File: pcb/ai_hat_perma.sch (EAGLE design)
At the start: 285 parts, among them J1 1X01-SM, J10 1X01-SM, J100 1X01-SM, J101 1X01-SM, J102 1X01-SM, J103 1X01-SM, J104 1X01-SM, J105 1X01-SM, J106 1X01-SM, J107 1X01-SM, J108 1X01-SM, J109 1X01-SM, J11 1X01-SM, J110 1X01-SM, J111 1X01-SM, J112 1X01-SM, J113 1X01-SM, J114 1X01-SM, J115 1X01-SM, J116 1X01-SM, J117 1X01-SM, J118 1X01-SM, J119 1X01-SM, J12 1X01-SM, J120 1X01-SM, J121 1X01-SM, J122 1X01-SM, J123 1X01-SM, J124 1X01-SM, J125 1X01-SM, J126 1X01-SM, J127 1X01-SM, J128 1X01-SM, J129 1X01-SM, J13 1X01-SM, J130 1X01-SM, J131 1X01-SM, J132 1X01-SM, J133 1X01-SM, J134 1X01-SM, J135 1X01-SM, J136 1X01-SM, J137 1X01-SM, J138 1X01-SM, J139 1X01-SM, J14 1X01-SM, J140 1X01-SM, J141 1X01-SM, J142 1X01-SM, J143 1X01-SM, J144 1X01-SM, J145 1X01-SM, J146 1X01-SM, J147 1X01-SM, J148 1X01-SM, J149 1X01-SM, J15 1X01-SM, J150 1X01-SM, J151 1X01-SM, J152 1X01-SM, J153 1X01-SM, J154 1X01-SM, J155 1X01-SM, J156 1X01-SM, J157 1X01-SM, J158 1X01-SM, J159 1X01-SM, J16 1X01-SM, J160 1X01-SM, J161 1X01-SM, J162 1X01-SM, J163 1X01-SM, J164 1X01-SM, J165 1X01-SM, J166 1X01-SM, J167 1X01-SM, J168 1X01-SM, J169 1X01-SM, J17 1X01-SM, J170 1X01-SM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

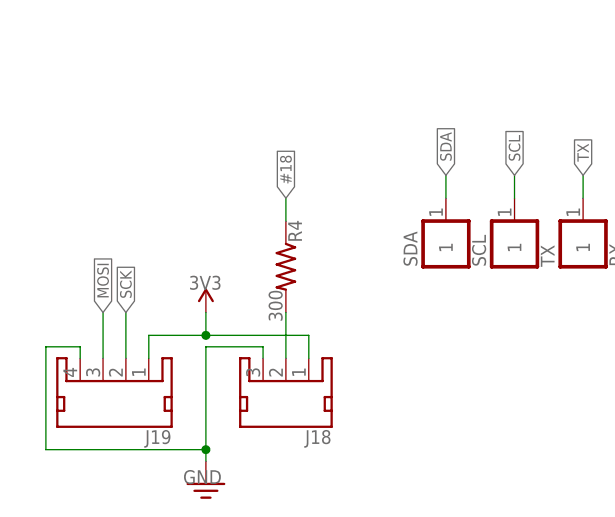
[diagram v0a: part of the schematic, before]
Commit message: updating supply to LEDs
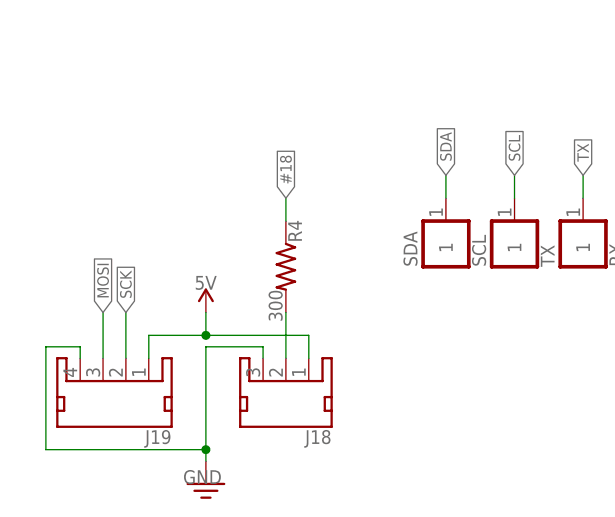
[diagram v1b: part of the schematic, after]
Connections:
- net 3V3: no longer J18.1, J19.1
- net 5V: now also J18.1, J19.1
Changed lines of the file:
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@@
 <part name="GND6" library="Ai_Power" deviceset="GND" device=""/>
 <part name="J19" library="Ai_Connectors" deviceset="JST-4P-MALE" device=""/>
-<part name="U$8" library="Ai_Power" deviceset="3V3" device=""/>
 <part name="GND7" library="Ai_Power" deviceset="GND" device=""/>
 <part name="R4" library="Ai_Passives" deviceset="RES" device="0603" value="300"/>
@@
 <part name="U$9" library="Ai_Miscellany" deviceset="AI-LOGO" device="XS"/>
 <part name="U$10" library="Ai_Miscellany" deviceset="AI-LOGO" device="XS"/>
+<part name="U$8" library="Ai_Power" deviceset="5V" device=""/>
 </parts>
 <sheets>
@@
 <instance part="GND6" gate="GND" x="246.38" y="158.75" rot="MR0"/>
 <instance part="J19" gate="G$1" x="12.7" y="13.97" rot="R180"/>
-<instance part="U$8" gate="G$1" x="22.86" y="24.13"/>
 <instance part="GND7" gate="GND" x="22.86" y="5.08"/>
 <instance part="R4" gate="G$1" x="31.75" y="29.21" rot="R270"/>
@@
 <instance part="U$9" gate="G$1" x="139.7" y="16.51"/>
 <instance part="U$10" gate="G$1" x="139.7" y="16.51"/>
+<instance part="U$8" gate="G$1" x="22.86" y="24.13"/>
 </instances>
 <busses>
@@
 <pinref part="U$6" gate="G$1" pin="5V"/>
 </segment>
+<segment>
+<pinref part="J19" gate="G$1" pin="1"/>
+<wire x1="16.51" y1="19.05" x2="16.51" y2="21.59" width="0.1524" layer="91"/>
+<wire x1="16.51" y1="21.59" x2="22.86" y2="21.59" width="0.1524" layer="91"/>
+<wire x1="22.86" y1="21.59" x2="22.86" y2="24.13" width="0.1524" layer="91"/>
+<pinref part="J18" gate="G$1" pin="1"/>
+<wire x1="34.29" y1="19.05" x2="34.29" y2="21.59" width="0.1524" layer="91"/>
+<wire x1="22.86" y1="21.59" x2="34.29" y2="21.59" width="0.1524" layer="91"/>
+<junction x="22.86" y="21.59"/>
+<pinref part="U$8" gate="G$1" pin="5V"/>
+</segment>
 </net>
 <net name="3V3" class="0">
@@
 <pinref part="U$7" gate="G$1" pin="3V3"/>
 </segment>
-<segment>
-<pinref part="J19" gate="G$1" pin="1"/>
-<wire x1="16.51" y1="19.05" x2="16.51" y2="21.59" width="0.1524" layer="91"/>
-<wire x1="16.51" y1="21.59" x2="22.86" y2="21.59" width="0.1524" layer="91"/>
-<pinref part="U$8" gate="G$1" pin="3V3"/>
-<wire x1="22.86" y1="21.59" x2="22.86" y2="24.13" width="0.1524" layer="91"/>
-<pinref part="J18" gate="G$1" pin="1"/>
-<wire x1="34.29" y1="19.05" x2="34.29" y2="21.59" width="0.1524" layer="91"/>
-<wire x1="22.86" y1="21.59" x2="34.29" y2="21.59" width="0.1524" layer="91"/>
-<junction x="22.86" y="21.59"/>
-</segment>
 </net>
